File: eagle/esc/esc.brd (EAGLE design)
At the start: 83.5 x 45.7 mm, 9 parts, among them IC1 DRV8305NPHPR, IC2 STM32L431CCT6LQFP48, J1 STLINK-PROG-CON, T1 CSD17573Q5B, T2 CSD17573Q5B, T3 CSD17573Q5B, T4 CSD17573Q5B, T5 CSD17573Q5B, T6 CSD17573Q5B

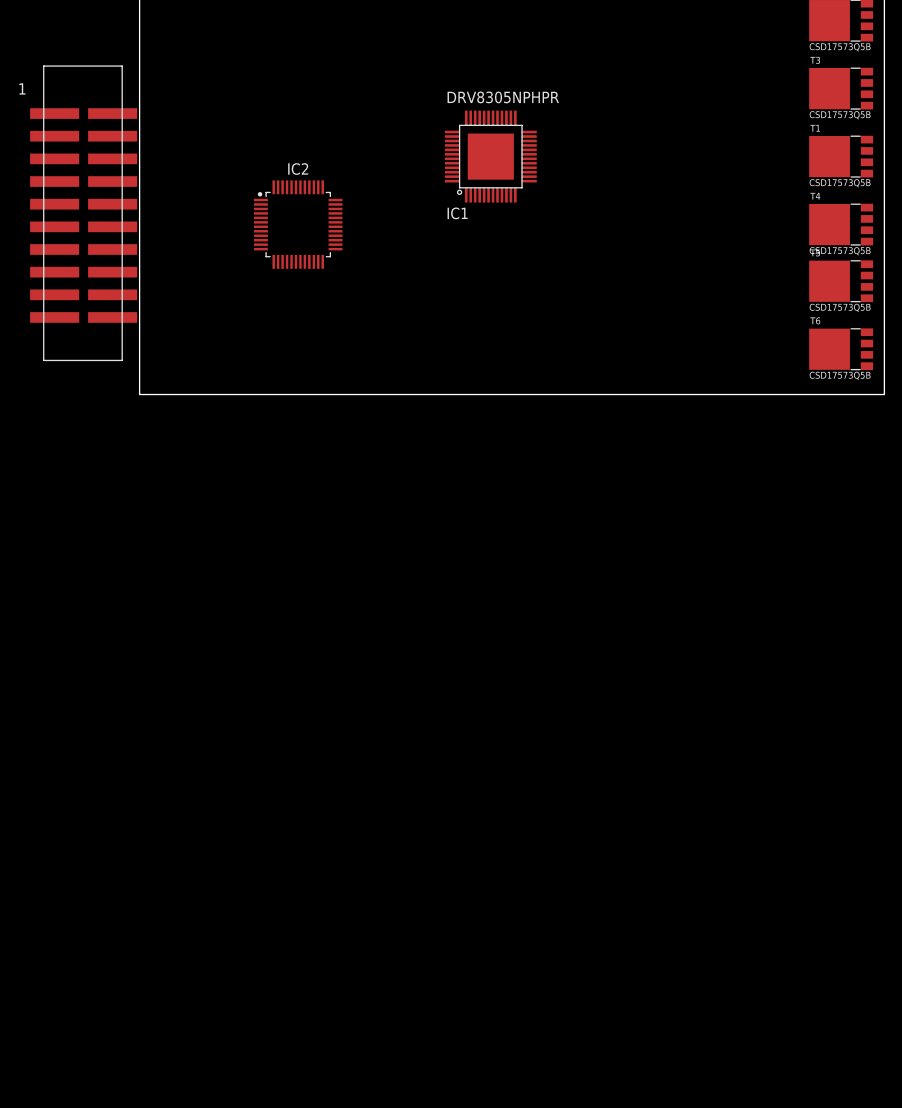
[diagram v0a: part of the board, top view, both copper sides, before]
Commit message: added FETs and related circuitry for the motor drive, current sense
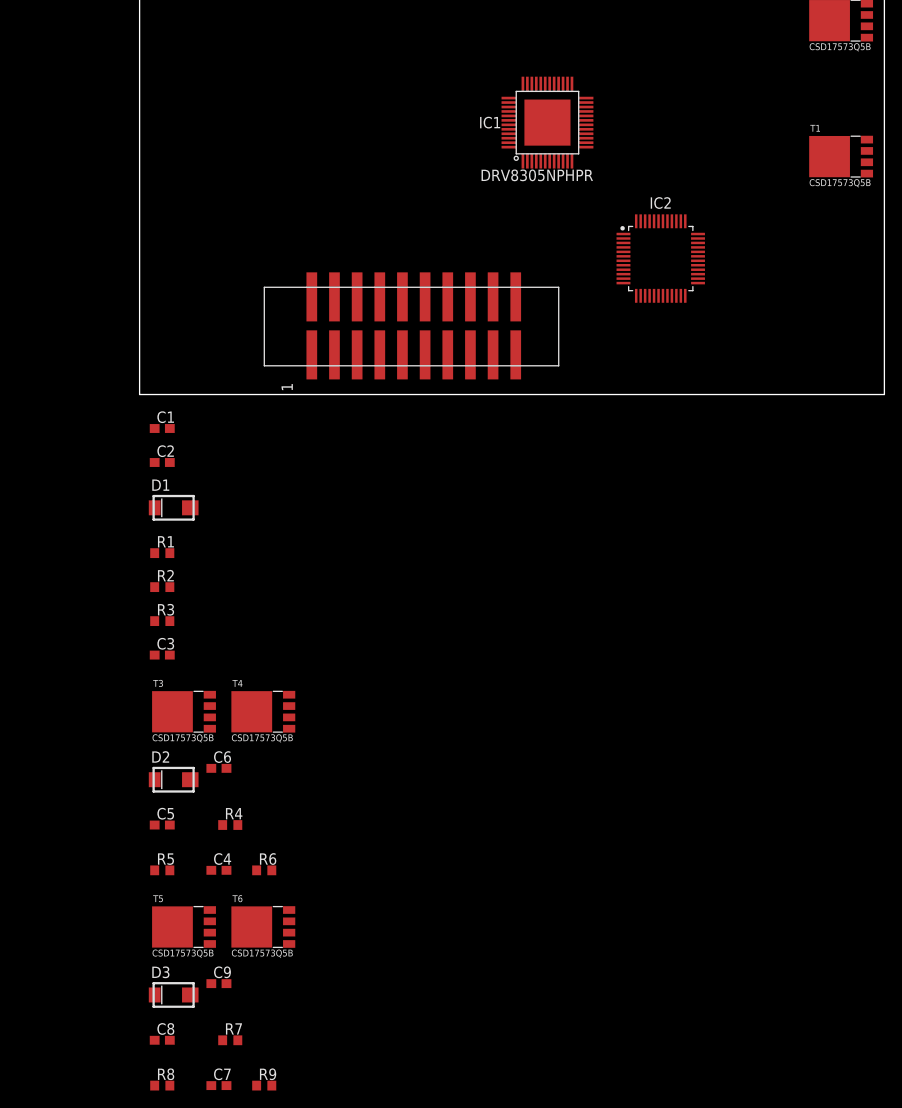
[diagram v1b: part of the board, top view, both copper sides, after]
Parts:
- added C1, C4, C7: 1 uF, resistor:C0603
- added C2, C5, C8: 0.1 uF, resistor:C0603
- added C3, C6, C9: 1000 pF, resistor:C0603
- added D1, D2, D3: (no value), diode:GF1
- added R1, R4, R7: 34.8k, resistor:R0603
- added R2, R5, R8: 4.99k, resistor:R0603
- added R3, R6, R9: 5 m, resistor:R0603
- moved T5 103.3 mm to (5.08, -59.7)
- moved T3 101.5 mm to (5.08, -35.6)
- moved T6 91.6 mm to (14.0, -59.7)
- moved T4 84.7 mm to (14.0, -35.6)
- moved IC2 40.8 mm to (58.4, 15.2)
- moved J1 39.0 mm to (30.5, 7.62), turned to 90 degrees
- moved IC1 7.41 mm to (45.7, 30.5)
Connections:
- new net ASENSE: C2.1, C5.1, C8.1, D1.A, D2.A, D3.A, R1.1, R2.2, R4.1, R5.2, R7.1, R8.2
- new net GND: C1.2, C2.2, C3.2, C4.2, C5.2, C6.2, C7.2, C8.2, C9.2, R2.1, R3.1, R5.1, R6.1, R8.1, R9.1
- new net N$1: R1.2, T1.1, T1.2, T1.3, T2.5
- new net N$10: C9.1, R9.2, T6.1, T6.2, T6.3
- new net N$11: T5.4
- new net N$12: T6.4
- new net N$2: C3.1, R3.2, T2.1, T2.2, T2.3
- new net N$3: T1.4
- new net N$4: T2.4
- new net N$5: R4.2, T3.1, T3.2, T3.3, T4.5
- new net N$6: C6.1, R6.2, T4.1, T4.2, T4.3
- new net N$7: T3.4
- new net N$8: T4.4
- new net N$9: R7.2, T5.1, T5.2, T5.3, T6.5
- new net VCC: D1.C, D2.C, D3.C
- new net VDD: C1.1, C4.1, C7.1, T1.5, T3.5, T5.5

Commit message: Added most of the components to the schematic. Left to add connectors for SPI port for micro and power connectors
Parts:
- removed J1: STLINK-PROG-CON, qc_esc:CON-20PIN-SMD
- added C10: 470 uF, rcl:E5-10,5
- added C11: 470 uF, rcl:E5-13
- added C12: 4.7 uF, resistor:C0805
- added C13, C17, C18, C19, C25, C28, C30, C32, C34: 1 uF, resistor:C0603
- added C14, C16: 0.047 uF, resistor:C0603
- added C15, C27: 2.2 uF, resistor:C0603
- added C20, C22, C26, C36: 0.1 uF, resistor:C0603
- added C21: 0.01 uF, resistor:C0603
- added C23: 10 uF, qc_esc:CAPAE430X580N
- added C24: CAPACITOR4.3X4.3, qc_esc:CAPAE430X580N
- added C29, C31, C33, C35: 100 nF, resistor:C0603
- added D4, D5: STPS2L30ASMA, qc_esc:DIOM5025X245N
- added J2: ARM10-CON, qc_esc:10-PIN-1.27-PITCH
- added LED1, LED2, LED3, LED4: (no value), eagle-ltspice:LED_SML0603
- added R10: 100, resistor:R0603
- added R11, R12: 10 k, resistor:R0603
- added R13: 34.8k, resistor:R0603
- added R14: 4.99k, resistor:R0603
- added R15, R16, R17, R18: 10k, resistor:R0603
- added R19: DNP, resistor:R0603
- added R20, R21, R22, R23: 1k, resistor:R0603
- added S1: (no value), switch-omron:B3F-10XX
- added U1: LD1117S50TR1, qc_esc:SOT230P700X180-4N
- added U2: MIC5319-3.3YD5-TR, qc_esc:SOT95P290X110-5N
- D1, D2, D3: value (none) -> STPS2L30ASMA; device diode:GF1 -> qc_esc:DIOM5025X245N
- moved D2 59.7 mm to (6.35, 16.5)
- moved T2 9.16 mm to (73.7, 34.3)
- moved T1 5.08 mm to (73.7, 26.7)
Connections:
- new net +5V: C24.1, D5.2, U1.2, U1.4
- new net BSENSE: C5.1, D2.2, R4.1, R5.2
- new net CSENSE: C8.1, D3.2, R7.1, R8.2
- new net EN_GATE: IC1.1
- new net GH_A: IC1.36, T1.4
- new net GH_B: IC1.29, T3.4
- new net GH_C: IC1.28, T5.4
- new net GL_A: IC1.33, T2.4
- new net GL_B: IC1.32, T4.4
- new net GL_C: IC1.25, T6.4
- new net INHA: IC1.2
- new net INHB: IC1.4
- new net INHC: IC1.6
- new net INLA: IC1.3
- new net INLB: IC1.5
- new net INLC: IC1.7
- new net N$13: IC2.44, R19.2
- new net N$14: LED1.A, R20.2
- new net N$16: LED2.A, R21.2
- new net N$17: LED3.A, R22.2
- new net N$18: LED4.A, R23.2
- new net NFAULT: IC1.8, R12.1
- new net NRST: C36.1, IC2.7, J2.10, S1.3, S1.4
- new net NSCS: IC1.9
- new net PVDDSENSE: C22.1, D4.2, R13.1, R14.2
- new net PWRGD: IC1.13, R11.1
- new net SCLK: IC1.12
- new net SDI: IC1.10
- new net SDO: IC1.11
- new net SH_A: IC1.35, R1.2, T1.1, T1.2, T1.3, T2.5
- new net SH_B: IC1.30, R4.2, T3.1, T3.2, T3.3, T4.5
- new net SH_C: IC1.27, R7.2, T5.1, T5.2, T5.3, T6.5
- new net SL_A: C3.1, IC1.34, R3.2, T2.1, T2.2, T2.3
- new net SL_B: C6.1, IC1.31, R6.2, T4.1, T4.2, T4.3
- new net SL_C: C9.1, IC1.26, R9.2, T6.1, T6.2, T6.3
- new net SN1: IC1.23
- new net SN2: IC1.21
- new net SN3: IC1.19
- new net SO1: IC1.16
- new net SO2: IC1.17
- new net SO3: IC1.18
- new net SP1: IC1.24
- new net SP2: IC1.22
- new net SP3: IC1.20
- new net STS1: LED2.C
- new net STS2: LED3.C
- new net STS3: LED4.C
- new net TCK: J2.4, R16.1
- new net TDI: J2.8, R18.1
- new net TDO: J2.6, R17.1
- new net TMS: J2.2, R15.1
- net ASENSE: now also D1.2; no longer C5.1, C8.1, D1.A, D2.A, D3.A, R4.1, R5.2, R7.1, R8.2
- net GND: now also C10.-, C11.-, C12.2, C13.2, C17.2, C18.1, C19.1, C20.1, C21.1, C22.2, C23.2, C24.2, C25.2, C26.2, C27.2, C28.2, C29.2, C30.2, C31.2, C32.2, C33.2, C34.2, C35.2, C36.2, IC1.14, IC1.45, IC1.49, IC2.23, IC2.35, IC2.47, IC2.8, J2.3, J2.5, J2.9, LED1.C, R14.1, R19.1, S1.1, S1.2, U1.1, U2.2
- net N$1: now also C13.1, IC1.37; no longer R1.2, T1.1, T1.2, T1.3, T2.5
- net N$10: now also C19.2, IC1.15; no longer C9.1, R9.2, T6.1, T6.2, T6.3
- net N$11: now also C25.1, D5.1, U2.1, U2.3; no longer T5.4
- net N$12: now also C26.1, U2.4; no longer T6.4
- net N$2: now also C16.1, IC1.42; no longer C3.1, R3.2, T2.1, T2.2, T2.3
- net N$3: now also C14.2, IC1.39; no longer T1.4
- net N$4: now also C14.1, IC1.40; no longer T2.4
- net N$5: now also C15.1, IC1.38; no longer R4.2, T3.1, T3.2, T3.3, T4.5
- net N$6: now also C16.2, IC1.43; no longer C6.1, R6.2, T4.1, T4.2, T4.3
- net N$7: now also C18.2, IC1.48; no longer T3.4
- net N$8: now also IC1.44, R10.1; no longer T4.4
- net N$9: now also C17.1, IC1.46; no longer R7.2, T5.1, T5.2, T5.3, T6.5
- net VCC: now also C27.1, C28.1, C29.1, C30.1, C31.1, C32.1, C33.1, C34.1, C35.1, D1.1, D2.1, D3.1, D4.1, IC2.1, IC2.24, IC2.36, IC2.48, IC2.9, J2.1, R11.2, R12.2, R15.2, R16.2, R17.2, R18.2, R20.1, R21.1, R22.1, R23.1, U2.5; no longer D1.C, D2.C, D3.C
- net VDD: now also C10.+, C11.+, C12.1, C15.2, C20.2, C21.2, C23.1, IC1.41, R10.2, R13.2, U1.3

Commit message: completed schematic of esc
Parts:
- added C37, C38: 0.1 uF, resistor:C0603
- added C39: 10 uF, resistor:CT3216
- added IC3: FT232RL, ftdichip:SSOP28
- added R24, R25: (no value), resistor:R0603
- added X1: C-GRID-02-15-19, con-molex:15-91-02
- added X2: MINI-USB-32005-301, con-cypressindustries:32005-301
- moved LED3 220.1 mm to (-22.9, -48.3)
- moved LED4 220.1 mm to (-22.9, -68.6)
- moved C25 220.1 mm to (-22.9, 25.4)
- moved C26 220.1 mm to (-22.9, 21.6)
- moved C27 220.1 mm to (-22.9, 17.8)
- moved C31 220.1 mm to (-22.9, 3.81)
- moved C33 220.1 mm to (-22.9, -6.35)
- moved C34 220.1 mm to (-22.9, -21.6)
- moved C35 220.1 mm to (-22.9, -16.5)
- moved C36 220.1 mm to (-22.9, -31.8)
- moved LED1 220.1 mm to (-22.9, -38.1)
- moved R15 220.1 mm to (-22.9, 41.9)
- moved R16 220.1 mm to (-22.9, 38.1)
- moved C28 220.1 mm to (-22.9, 12.7)
- moved C29 220.1 mm to (-22.9, 8.89)
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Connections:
- removed net SN1: IC1.23
- removed net SN2: IC1.21
- removed net SN3: IC1.19
- removed net SP1: IC1.24
- removed net SP2: IC1.22
- removed net SP3: IC1.20
- new net I2C_SCL: IC2.45, R24.1, X1.1
- new net I2C_SDA: IC2.46, R25.1, X1.2
- new net N$15: C37.1, C39.-, IC3.20, X2.1
- new net N$19: C38.1, IC3.17, IC3.4
- new net N$20: IC3.16, X2.2
- new net N$21: IC3.15, X2.3
- new net NJTRST: IC2.40, J2.10
- new net UART_RX: IC2.43, IC3.5
- new net UART_TX: IC2.42, IC3.1
- net ASENSE: now also IC2.17
- net BSENSE: now also IC2.18
- net CSENSE: now also IC2.19
- net EN_GATE: now also IC2.20
- net GND: now also C37.2, C38.2, C39.+, IC1.20, IC1.22, IC1.24, IC3.18, IC3.21, IC3.25, IC3.26, IC3.7, X2.5
- net INHA: now also IC2.29
- net INHB: now also IC2.30
- net INHC: now also IC2.31
- net INLA: now also IC2.10
- net INLB: now also IC2.11
- net INLC: now also IC2.12
- net NFAULT: now also IC2.21
- net NRST: no longer J2.10
- net NSCS: now also IC2.25
- net PVDDSENSE: now also IC2.16
- net PWRGD: now also IC2.22
- net SCLK: now also IC2.26
- net SDI: now also IC2.28
- net SDO: now also IC2.27
- net SL_A: now also IC1.23
- net SL_B: now also IC1.21
- net SL_C: now also IC1.19
- net SO1: now also IC2.13
- net SO2: now also IC2.14
- net SO3: now also IC2.15
- net STS1: now also IC2.32
- net STS2: now also IC2.33
- net STS3: now also IC2.41
- net TCK: now also IC2.37
- net TDI: now also IC2.38
- net TDO: now also IC2.39
- net TMS: now also IC2.34
- net VCC: now also R24.2, R25.2
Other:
- board size 83.5 x 45.7 mm -> 101.3 x 50.8 mm

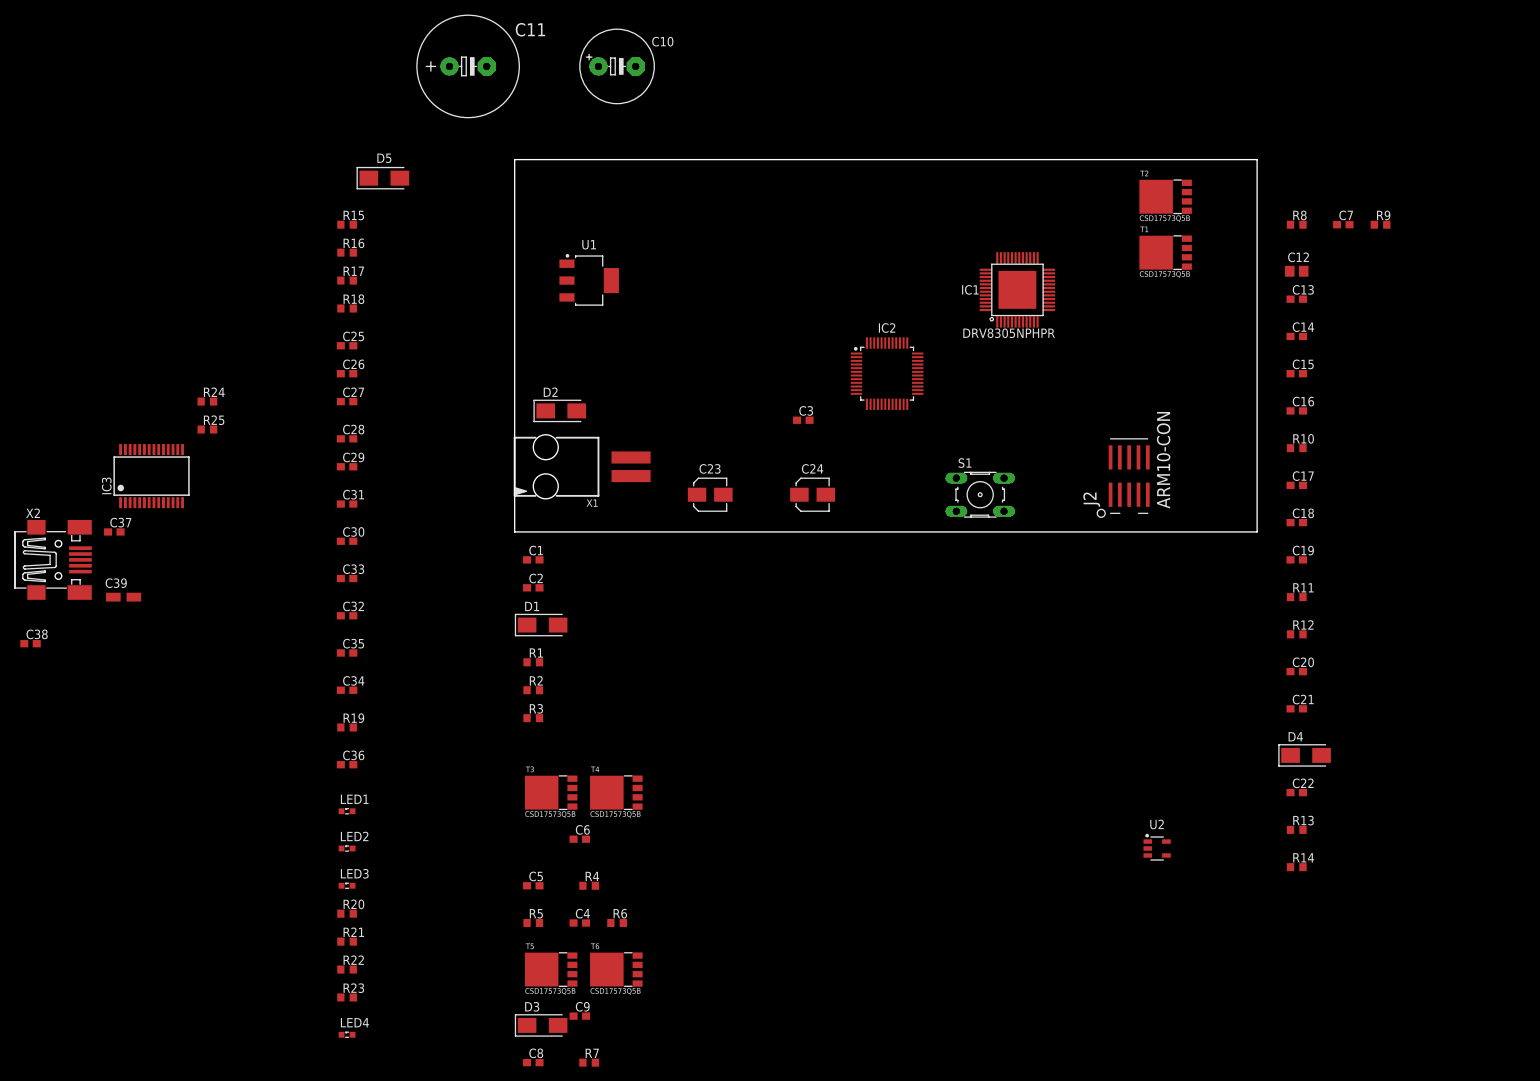
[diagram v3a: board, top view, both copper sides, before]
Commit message: Board layout save 1. Completed driver layout
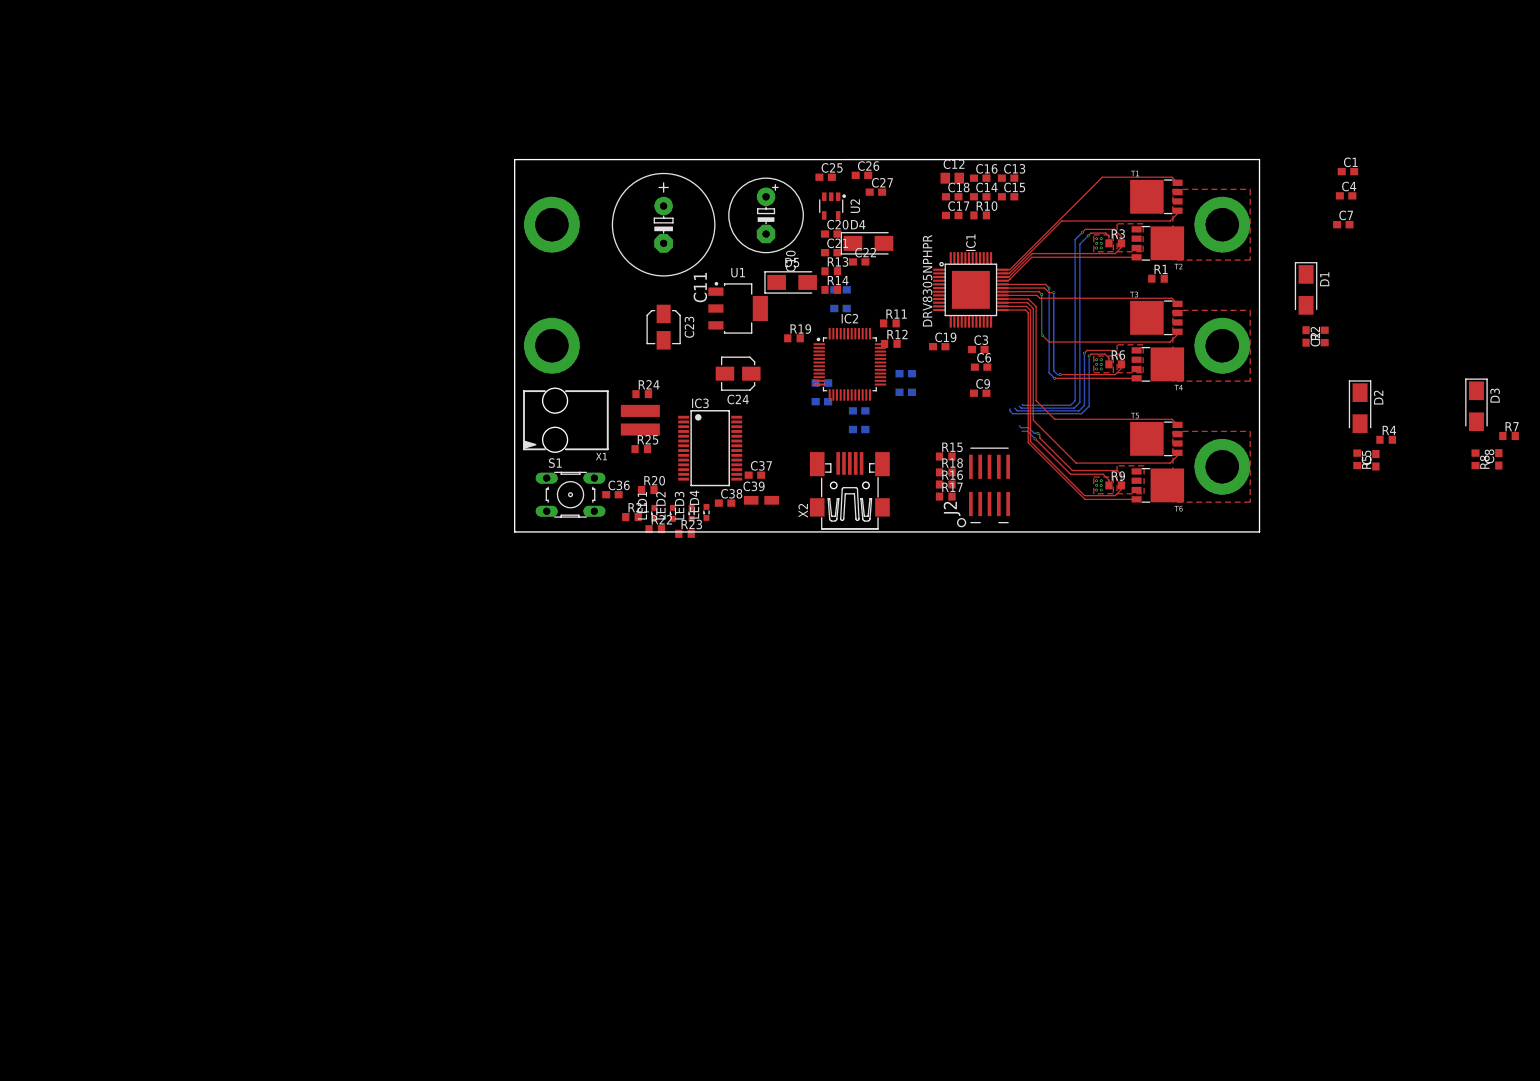
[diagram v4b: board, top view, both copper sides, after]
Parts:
- moved C8 155.3 mm to (134.2, 9.91), turned to 90 degrees
- moved D3 152.8 mm to (131.2, 17.1), turned to 270 degrees
- moved R7 151.8 mm to (135.6, 13.1)
- moved C4 144.1 mm to (113.4, 45.8)
- moved R5 129.0 mm to (114.9, 9.91), turned to 270 degrees
- moved C5 128.8 mm to (117.5, 9.78), turned to 90 degrees
- moved R4 124.6 mm to (118.9, 12.6)
- moved C1 123.1 mm to (113.7, 49.1)
- moved R2 118.2 mm to (110.5, 26.7), turned to 90 degrees
- moved D1 113.7 mm to (108.0, 33.0), turned to 270 degrees
- moved C2 110.8 mm to (108.0, 26.7), turned to 270 degrees
- moved T5 109.8 mm to (87.6, 12.7)
- moved D2 109.0 mm to (115.3, 16.9), turned to 270 degrees
- moved X2 108.4 mm to (45.7, 6.35), turned to 90 degrees
- moved T3 104.9 mm to (87.6, 29.2)
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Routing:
- net GND: track 0.00 -> 73.7 mm, vias 0 -> 22
- net SL_C: track 0.00 -> 56.7 mm, vias 0 -> 1
- net SL_A: track 0.00 -> 56.2 mm, vias 0 -> 1
- net SL_B: track 0.00 -> 51.9 mm, vias 0 -> 3
- net SH_C: track 0.00 -> 42.7 mm, vias 0 -> 1
- net GL_C: track 0.00 -> 39.4 mm
- net GH_C: track 0.00 -> 38.5 mm
- net SH_B: track 0.00 -> 30.7 mm, vias 0 -> 3
- net GL_B: track 0.00 -> 30.4 mm, vias 0 -> 2
- net GH_A: track 0.00 -> 29.4 mm
- net SH_A: track 0.00 -> 27.7 mm, vias 0 -> 1
- net GH_B: track 0.00 -> 24.4 mm
- net GL_A: track 0.00 -> 19.6 mm
- added copper zone on layer 1, net GND
- added copper zone on layer 2, net GND
- added copper zone on layer 1, net SH_A
- added copper zone on layer 1, net SH_B
- added copper zone on layer 1, net SH_C
- added copper zone on layer 1, net SL_A
- added copper zone on layer 1, net SL_B
- added copper zone on layer 1, net SL_C
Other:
- board size 101.3 x 50.8 mm -> 101.6 x 50.8 mm
